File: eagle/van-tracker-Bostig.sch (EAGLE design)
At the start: 14 parts, among them K1 CP1-12V, Q1 TIP122, Q2 TIP122

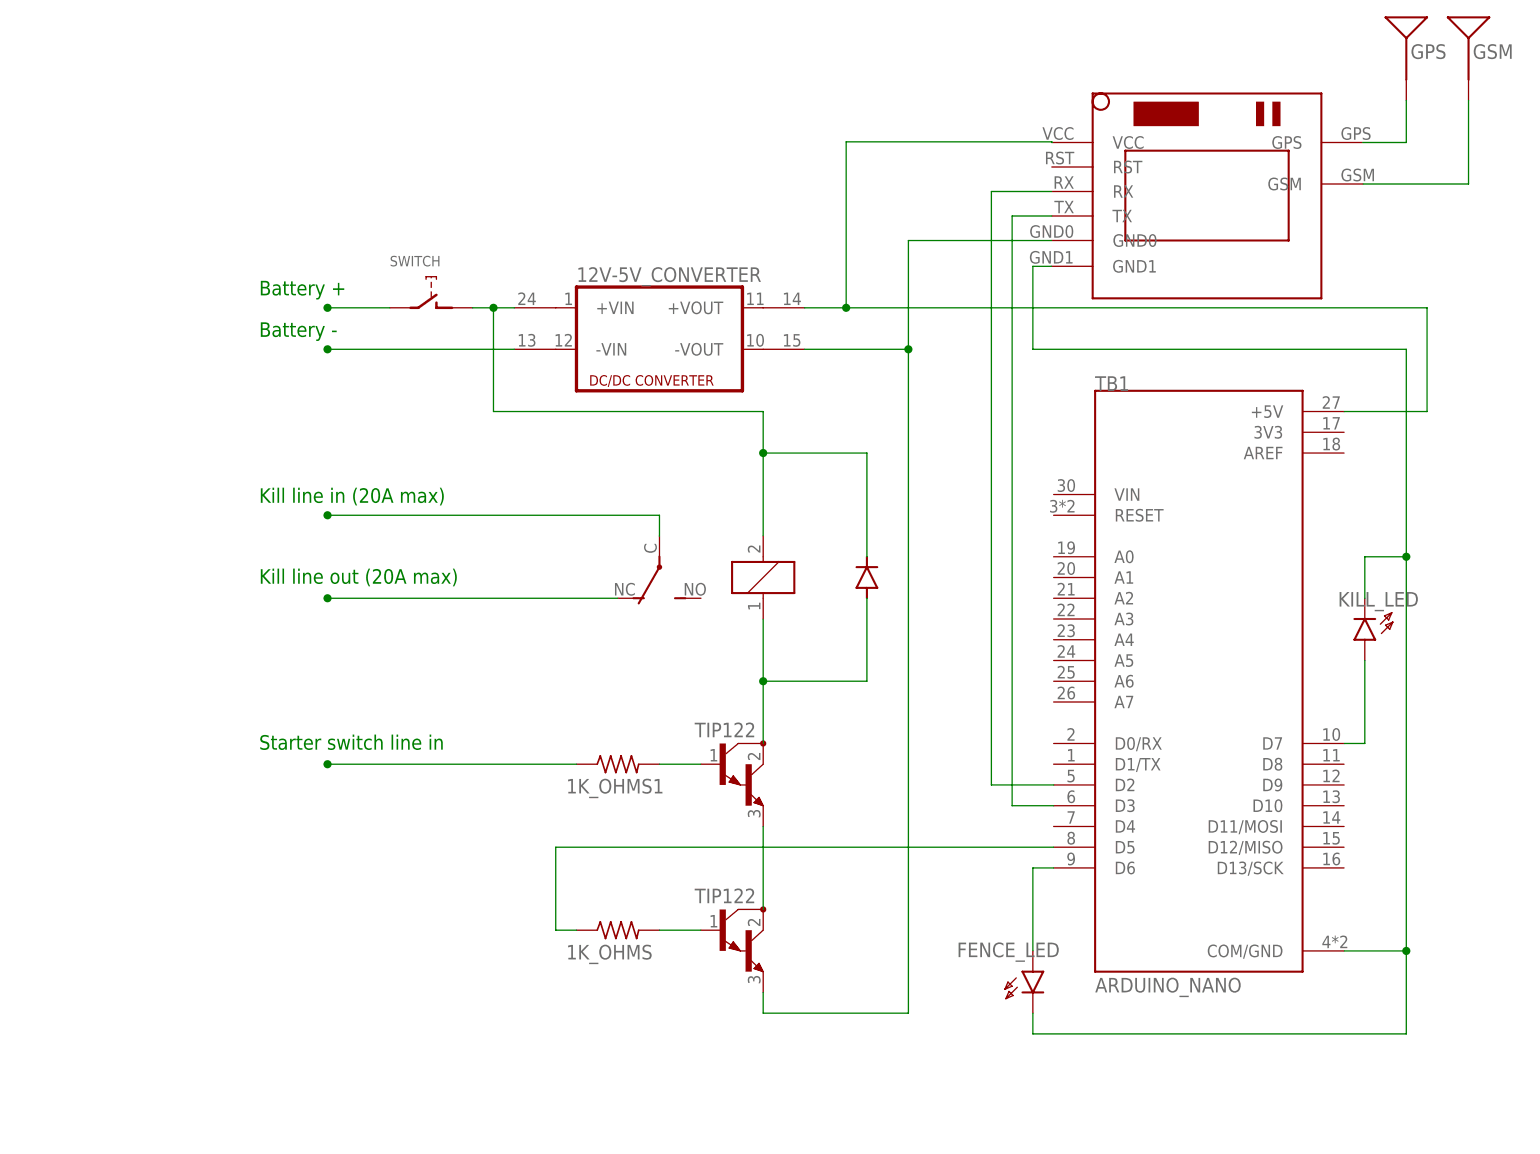
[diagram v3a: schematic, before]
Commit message: 1.add diode going to Arduino +5V pin so we can turn system off and update Arduino via USB. Removed fence and kill switch LEDs
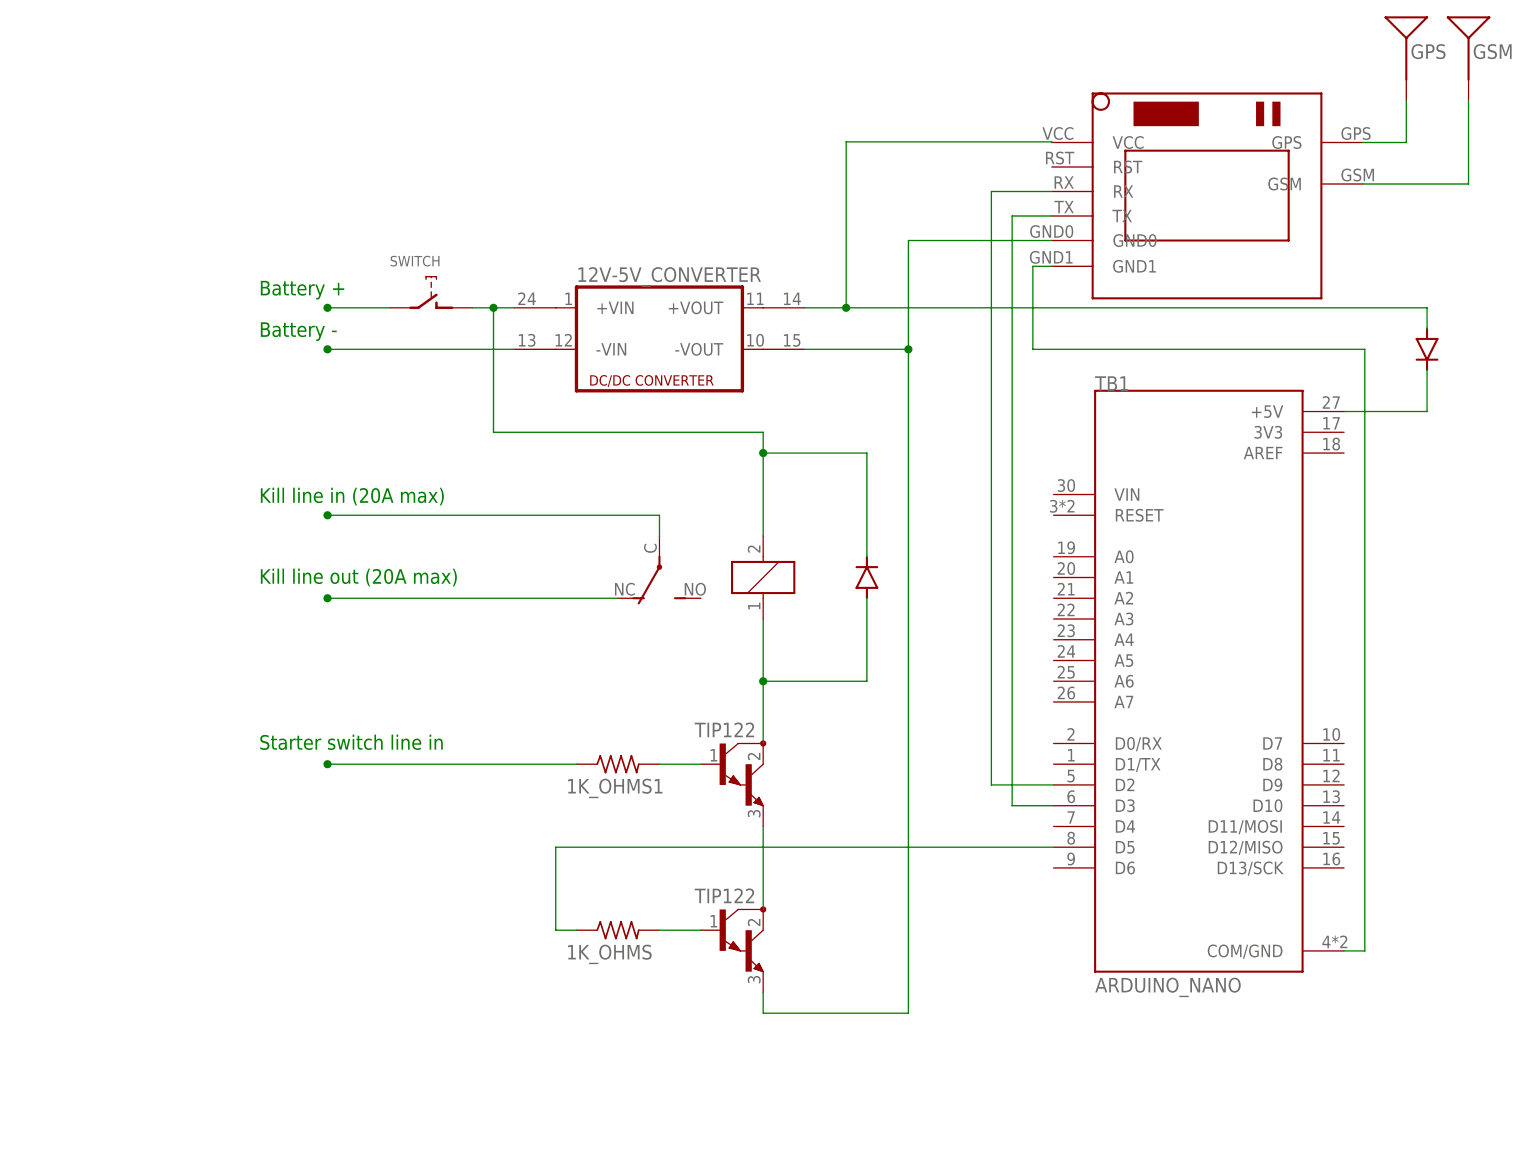
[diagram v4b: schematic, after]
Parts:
- removed FENCE_LED, KILL_LED: HLMP6, display-hp:HLMP6
- added D2: 1N5400, diode:1N5400
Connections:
- removed net N$14: KILL_LED.A, TB1.D7
- removed net N$15: FENCE_LED.A, TB1.D6
- new net N$10: D2.C, TB1.+5V
- net N$22: no longer FENCE_LED.K, KILL_LED.K
- net N$9: now also D2.A; no longer TB1.+5V
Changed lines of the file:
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@@
 <part name="U$1" library="JW_SIM800LMODULE" deviceset="SIM800LMODULE" device=""/>
 <part name="D1" library="diode" library_urn="urn:adsk.eagle:library:210" deviceset="1N5400" device="" package3d_urn="urn:adsk.eagle:package:43365/2"/>
-<part name="FENCE_LED" library="display-hp" library_urn="urn:adsk.eagle:library:212" deviceset="HLMP6" device="" package3d_urn="urn:adsk.eagle:package:12992/1"/>
-<part name="KILL_LED" library="display-hp" library_urn="urn:adsk.eagle:library:212" deviceset="HLMP6" device="" package3d_urn="urn:adsk.eagle:package:12992/1"/>
 <part name="1K_OHMS" library="rcl" library_urn="urn:adsk.eagle:library:334" deviceset="R-US_" device="0411/15" package3d_urn="urn:adsk.eagle:package:23568/2"/>
 <part name="SWITCH" library="switch-alps" library_urn="urn:adsk.eagle:library:373" deviceset="EC12E_SW" device="" package3d_urn="urn:adsk.eagle:package:27083/1"/>
@@
 <part name="1K_OHMS1" library="rcl" library_urn="urn:adsk.eagle:library:334" deviceset="R-US_" device="0411/15" package3d_urn="urn:adsk.eagle:package:23568/2"/>
 <part name="Q2" library="transistor-npn" library_urn="urn:adsk.eagle:library:398" deviceset="TIP122*" device="" package3d_urn="urn:adsk.eagle:package:28520/1"/>
+<part name="D2" library="diode" library_urn="urn:adsk.eagle:library:210" deviceset="1N5400" device="" package3d_urn="urn:adsk.eagle:package:43365/2"/>
 </parts>
 <sheets>
@@
 <instance part="U$1" gate="G$1" x="73.66" y="81.28" smashed="yes"/>
 <instance part="D1" gate="1" x="33.02" y="33.02" smashed="yes" rot="R90"/>
-<instance part="FENCE_LED" gate="A" x="53.34" y="-17.78" smashed="yes">
-<attribute name="NAME" x="56.642" y="-11.684" size="1.778" layer="95" rot="R180"/>
-</instance>
-<instance part="KILL_LED" gate="A" x="93.98" y="27.94" smashed="yes" rot="R180">
-<attribute name="NAME" x="90.678" y="29.464" size="1.778" layer="95"/>
-</instance>
 <instance part="1K_OHMS" gate="G$1" x="2.54" y="-10.16" smashed="yes">
 <attribute name="NAME" x="-3.81" y="-13.7414" size="1.778" layer="95"/>
@@
 <attribute name="VALUE" x="11.938" y="13.462" size="1.778" layer="96"/>
 </instance>
+<instance part="D2" gate="1" x="101.6" y="60.96" smashed="yes" rot="R270"/>
 </instances>
 <busses>
@@
 <wire x1="30.48" y1="66.04" x2="101.6" y2="66.04" width="0.1524" layer="91"/>
 <junction x="30.48" y="66.04"/>
-<wire x1="101.6" y1="66.04" x2="101.6" y2="53.34" width="0.1524" layer="91"/>
-<pinref part="TB1" gate="G$1" pin="+5V"/>
-<wire x1="101.6" y1="53.34" x2="91.44" y2="53.34" width="0.1524" layer="91"/>
+<pinref part="D2" gate="1" pin="A"/>
+<wire x1="101.6" y1="66.04" x2="101.6" y2="63.5" width="0.1524" layer="91"/>
 </segment>
 </net>
@@
 </segment>
 </net>
-<net name="N$14" class="0">
-<segment>
-<pinref part="TB1" gate="G$1" pin="D7"/>
-<pinref part="KILL_LED" gate="A" pin="A"/>
-<wire x1="91.44" y1="12.7" x2="93.98" y2="12.7" width="0.1524" layer="91"/>
-<wire x1="93.98" y1="12.7" x2="93.98" y2="22.86" width="0.1524" layer="91"/>
-</segment>
-</net>
-<net name="N$15" class="0">
-<segment>
-<pinref part="TB1" gate="G$1" pin="D6"/>
-<pinref part="FENCE_LED" gate="A" pin="A"/>
-<wire x1="55.88" y1="-2.54" x2="53.34" y2="-2.54" width="0.1524" layer="91"/>
-<wire x1="53.34" y1="-2.54" x2="53.34" y2="-12.7" width="0.1524" layer="91"/>
-</segment>
-</net>
 <net name="N$17" class="0">
 <segment>
@@
 <wire x1="-10.16" y1="66.04" x2="-12.7" y2="66.04" width="0.1524" layer="91"/>
 <wire x1="-12.7" y1="66.04" x2="-15.24" y2="66.04" width="0.1524" layer="91"/>
-<wire x1="-12.7" y1="66.04" x2="-12.7" y2="53.34" width="0.1524" layer="91"/>
+<wire x1="-12.7" y1="66.04" x2="-12.7" y2="50.8" width="0.1524" layer="91"/>
 <junction x="-12.7" y="66.04"/>
-<wire x1="-12.7" y1="53.34" x2="20.32" y2="53.34" width="0.1524" layer="91"/>
+<wire x1="-12.7" y1="50.8" x2="20.32" y2="50.8" width="0.1524" layer="91"/>
 <pinref part="K1" gate="1" pin="2"/>
 <wire x1="20.32" y1="48.26" x2="20.32" y2="38.1" width="0.1524" layer="91"/>
@@
 <wire x1="33.02" y1="35.56" x2="33.02" y2="48.26" width="0.1524" layer="91"/>
 <wire x1="33.02" y1="48.26" x2="20.32" y2="48.26" width="0.1524" layer="91"/>
-<wire x1="20.32" y1="53.34" x2="20.32" y2="48.26" width="0.1524" layer="91"/>
+<wire x1="20.32" y1="50.8" x2="20.32" y2="48.26" width="0.1524" layer="91"/>
 <junction x="20.32" y="48.26"/>
 </segment>
@@
 <net name="N$22" class="0">
 <segment>
-<wire x1="53.34" y1="60.96" x2="99.06" y2="60.96" width="0.1524" layer="91"/>
-<wire x1="99.06" y1="60.96" x2="99.06" y2="35.56" width="0.1524" layer="91"/>
+<wire x1="53.34" y1="60.96" x2="93.98" y2="60.96" width="0.1524" layer="91"/>
 <pinref part="TB1" gate="G$1" pin="COM/GND"/>
-<wire x1="99.06" y1="35.56" x2="99.06" y2="-12.7" width="0.1524" layer="91"/>
-<wire x1="99.06" y1="-12.7" x2="91.44" y2="-12.7" width="0.1524" layer="91"/>
-<pinref part="KILL_LED" gate="A" pin="K"/>
-<wire x1="93.98" y1="30.48" x2="93.98" y2="35.56" width="0.1524" layer="91"/>
-<wire x1="93.98" y1="35.56" x2="99.06" y2="35.56" width="0.1524" layer="91"/>
-<junction x="99.06" y="35.56"/>
-<pinref part="FENCE_LED" gate="A" pin="K"/>
-<wire x1="53.34" y1="-20.32" x2="53.34" y2="-22.86" width="0.1524" layer="91"/>
-<wire x1="53.34" y1="-22.86" x2="99.06" y2="-22.86" width="0.1524" layer="91"/>
-<wire x1="99.06" y1="-22.86" x2="99.06" y2="-12.7" width="0.1524" layer="91"/>
-<junction x="99.06" y="-12.7"/>
+<wire x1="93.98" y1="60.96" x2="93.98" y2="-12.7" width="0.1524" layer="91"/>
+<wire x1="93.98" y1="-12.7" x2="91.44" y2="-12.7" width="0.1524" layer="91"/>
 <pinref part="U$1" gate="G$1" pin="GND1"/>
 <wire x1="55.626" y1="71.12" x2="53.34" y2="71.12" width="0.1524" layer="91"/>
@@
 </segment>
 </net>
+<net name="N$10" class="0">
+<segment>
+<pinref part="TB1" gate="G$1" pin="+5V"/>
+<wire x1="101.6" y1="53.34" x2="91.44" y2="53.34" width="0.1524" layer="91"/>
+<pinref part="D2" gate="1" pin="C"/>
+<wire x1="101.6" y1="58.42" x2="101.6" y2="53.34" width="0.1524" layer="91"/>
+</segment>
+</net>

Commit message: 1.add input signal from starter to D2 using voltage divider in order to send text msg when attempt to start while kill switch is on
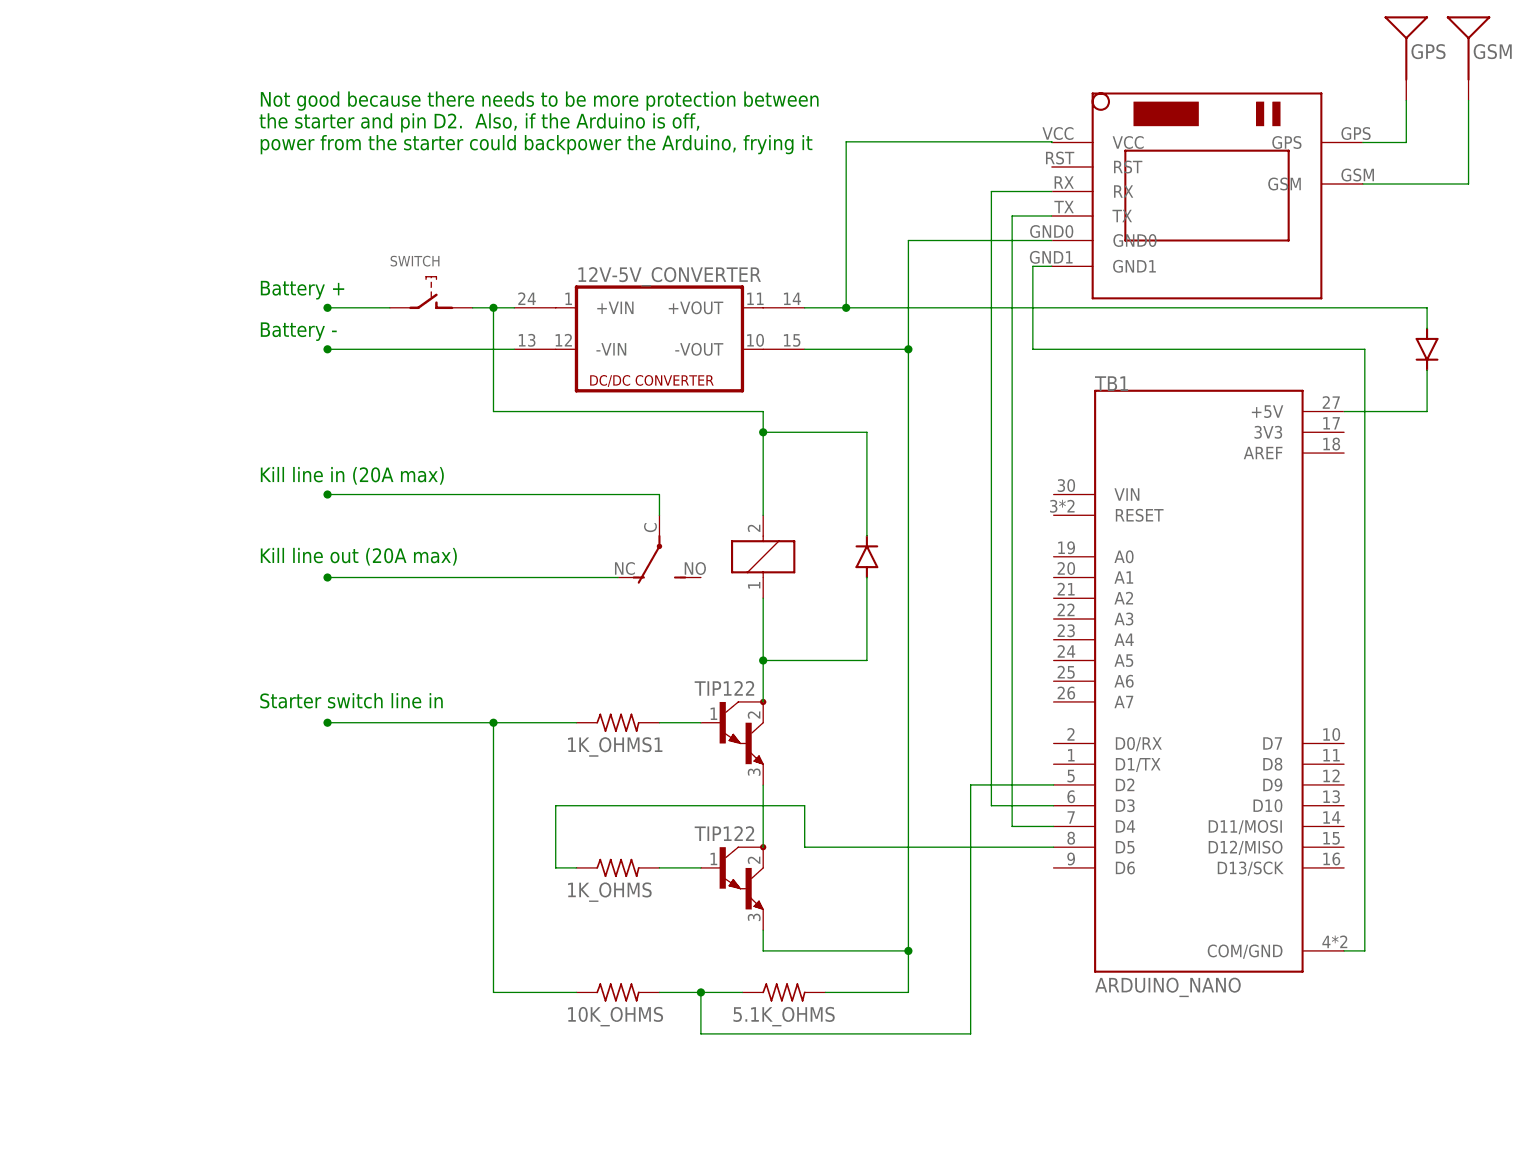
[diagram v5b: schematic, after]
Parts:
- added 10K_OHMS, 5.1K_OHMS: (no value), rcl:R-US_0411/15
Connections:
- new net N$15: 10K_OHMS.2, 5.1K_OHMS.1, TB1.D2
- net N$11: now also TB1.D3; no longer TB1.D2
- net N$12: now also TB1.D4; no longer TB1.D3
- net N$21: now also 10K_OHMS.1
- net N$23: now also 5.1K_OHMS.2
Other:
- note added: "Not good because there needs to be more protection between the starter and pin D2. Also, if the Arduino is off, power from the starter could backpower the Arduino, frying it"
- moved on the sheet: 1K_OHMS, 1K_OHMS1

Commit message: 1.Bostig: change voltage divider to transistor. use INPUT_PULLUP in software, so when signal to base of transistor is hot, arduino pin is pulled low. seems like the best way to protect arduino from car voltage spikes
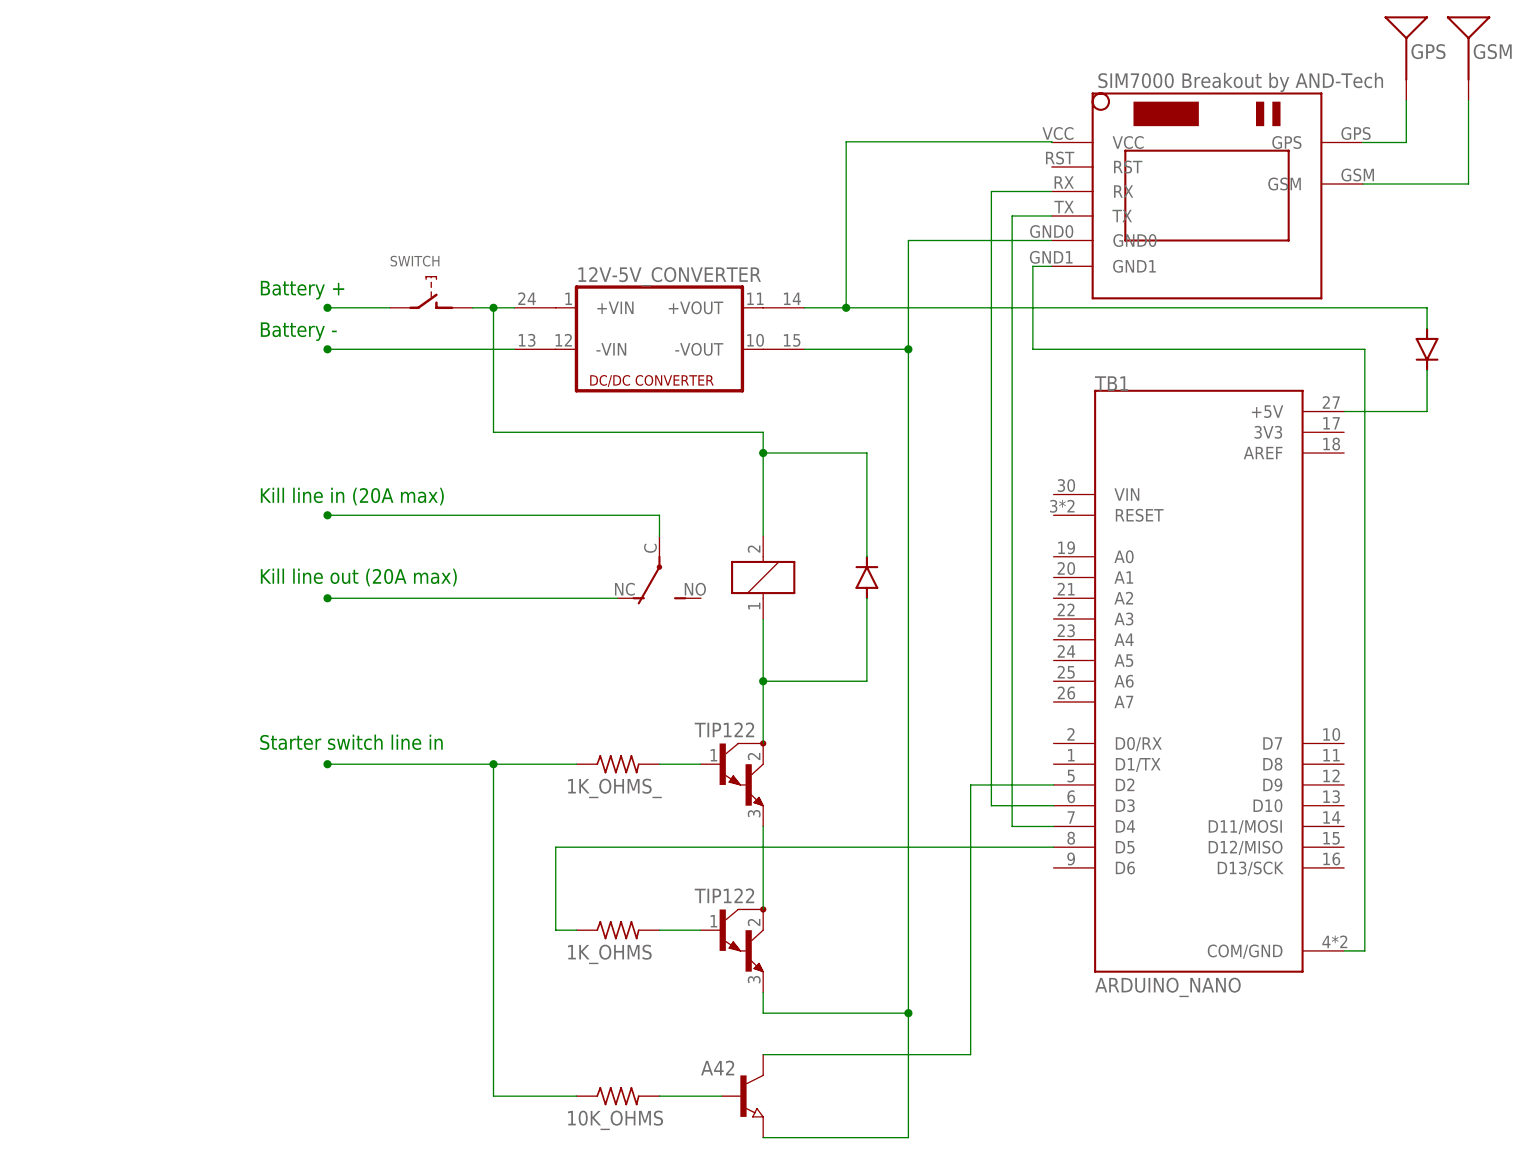
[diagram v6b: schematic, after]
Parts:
- removed 1K_OHMS1, 5.1K_OHMS: (no value), rcl:R-US_0411/15
- added 1K_OHMS_: (no value), rcl:R-US_0411/15
- added A42: (no value), semicon-smd-ipc:NPN-TRANSISTOR_SOT23
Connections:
- new net N$14: 10K_OHMS.2, A42.B
- net N$13: now also 1K_OHMS_.2; no longer 1K_OHMS1.2
- net N$15: now also A42.C; no longer 10K_OHMS.2, 5.1K_OHMS.1
- net N$21: now also 1K_OHMS_.1; no longer 1K_OHMS1.1
- net N$23: now also A42.E; no longer 5.1K_OHMS.2
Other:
- note removed: "Not good because there needs to be more protection between the starter and pin D2. Also, if the Arduino is off, power from the starter could backpower the Arduino, frying it"
- moved on the sheet: 10K_OHMS, 1K_OHMS
